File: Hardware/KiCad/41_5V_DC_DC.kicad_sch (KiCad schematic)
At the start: 0 parts

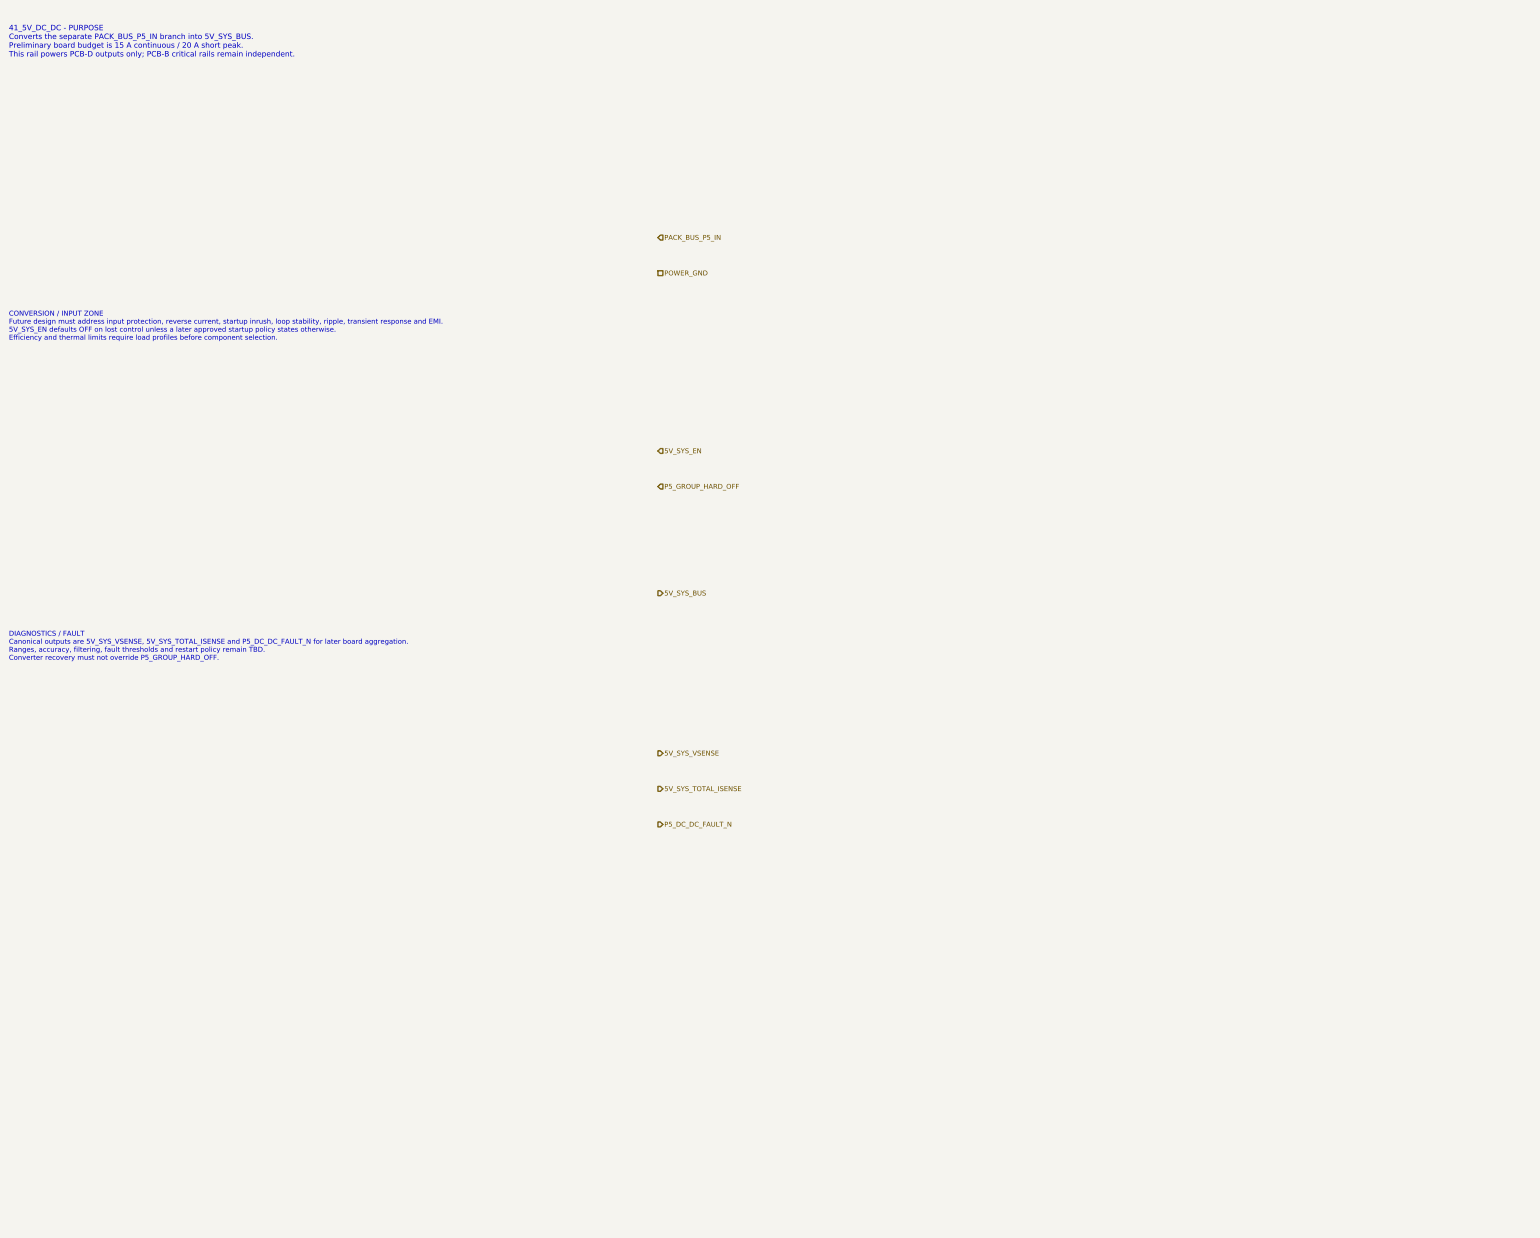
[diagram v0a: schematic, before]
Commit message: hardware: define PCB-D converter core after calculation gate
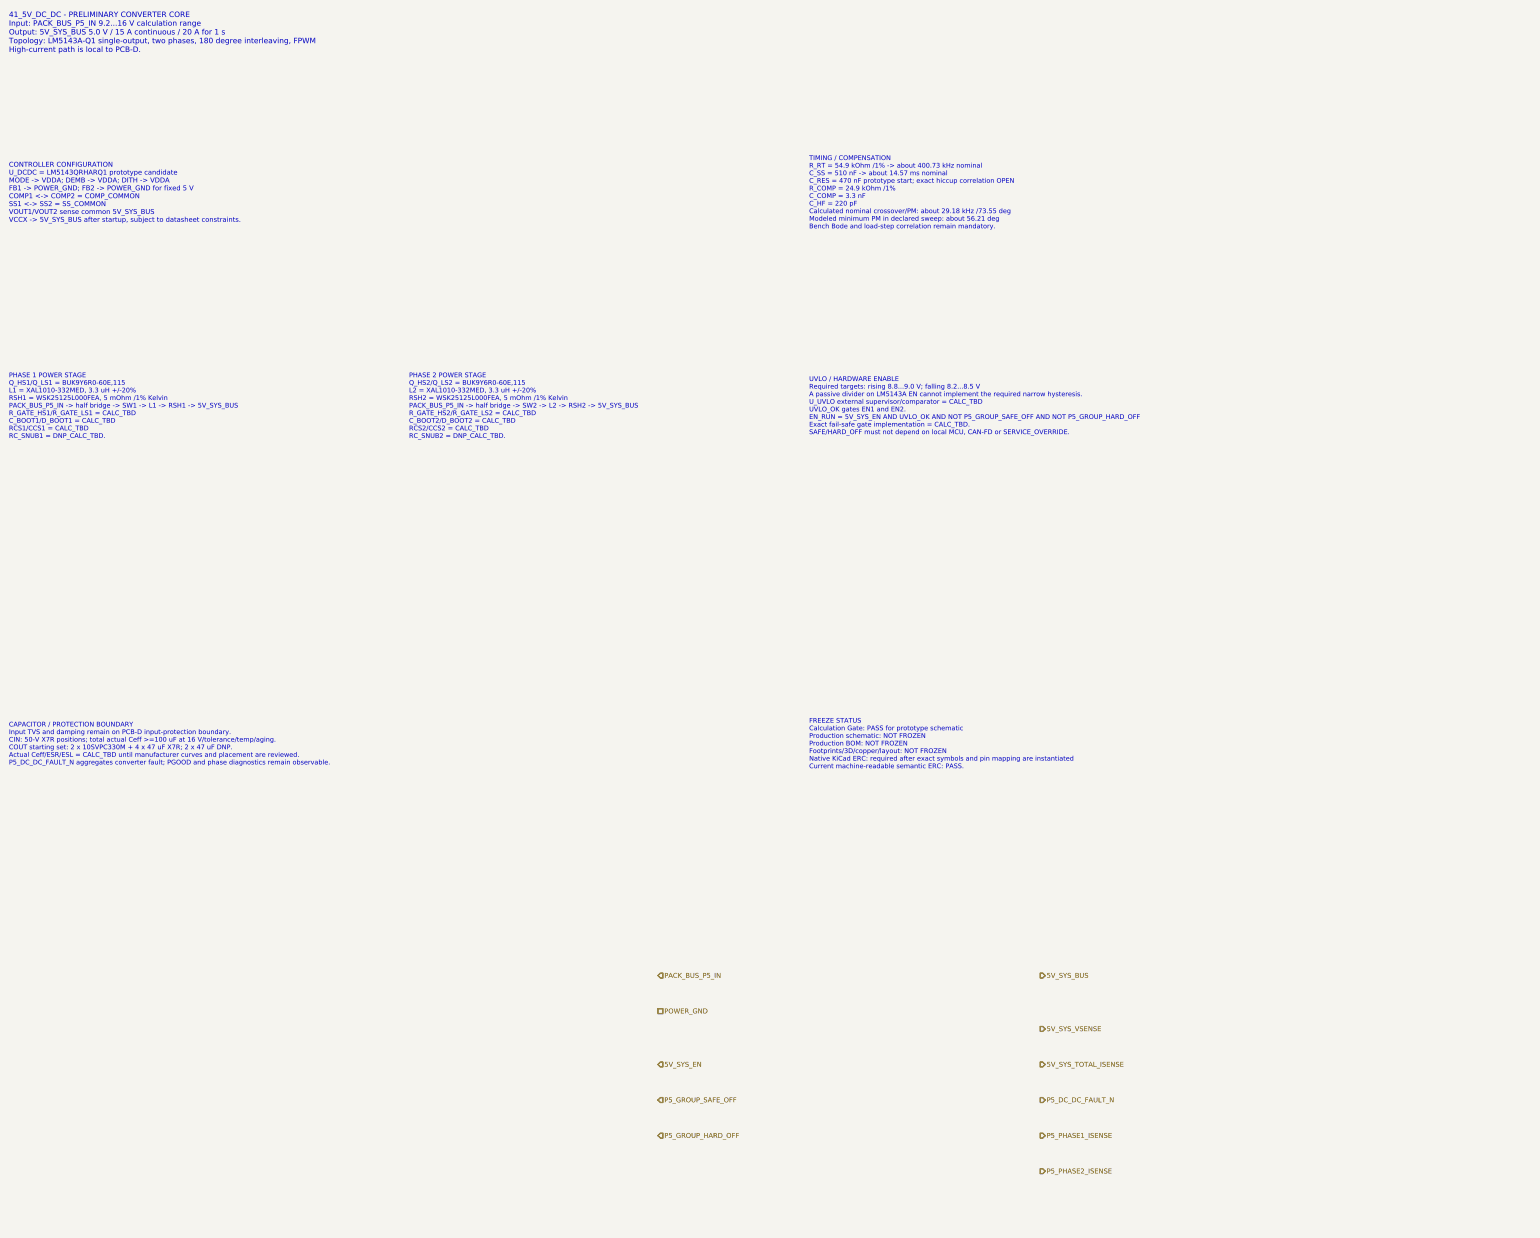
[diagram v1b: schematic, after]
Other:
- note added: "41_5V_DC_DC - PRELIMINARY CONVERTER CORE Input: PACK_BUS_P5_IN 9.2...16 V calculation range Output: 5V_SYS_BUS 5.0 V / 15 A continuous / 20 A for 1 s Topology: LM5143A-Q1 single-output, two phases, 180 degree interleaving, FPWM High-current path is local to PCB-D."
- note added: "CAPACITOR / PROTECTION BOUNDARY Input TVS and damping remain on PCB-D input-protection boundary. CIN: 50-V X7R positions; total actual Ceff >=100 uF at 16 V/tolerance/temp/aging. COUT starting set: 2 x 10SVPC330M + 4 x 47 uF X7R; 2 x 47 uF DNP. Actual Ceff/ESR/ESL = CALC_TBD until manufacturer curves and placement are reviewed. P5_DC_DC_FAULT_N aggregates converter fault; PGOOD and phase diagnost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"
- note added: "CONTROLLER CONFIGURATION U_DCDC = LM5143QRHARQ1 prototype candidate MODE -> VDDA; DEMB -> VDDA; DITH -> VDDA FB1 -> POWER_GND; FB2 -> POWER_GND for fixed 5 V COMP1 <-> COMP2 = COMP_COMMON SS1 <-> SS2 = SS_COMMON VOUT1/VOUT2 sense common 5V_SYS_BUS VCCX -> 5V_SYS_BUS after startup, subject to datasheet constraints."
- note added: "FREEZE STATUS Calculation Gate: PASS for prototype schematic Production schematic: NOT FROZEN Production BOM: NOT FROZEN Footprints/3D/copper/layout: NOT FROZEN Native KiCad ERC: required after exact symbols and pin mapping are instantiated Current machine-readable semantic ERC: PASS."
- note added: "PHASE 1 POWER STAGE Q_HS1/Q_LS1 = BUK9Y6R0-60E,115 L1 = XAL1010-332MED, 3.3 uH +/-20% RSH1 = WSK25125L000FEA, 5 mOhm /1% Kelvin PACK_BUS_P5_IN -> half bridge -> SW1 -> L1 -> RSH1 -> 5V_SYS_BUS R_GATE_HS1/R_GATE_LS1 = CALC_TBD C_BOOT1/D_BOOT1 = CALC_TBD RCS1/CCS1 = CALC_TBD RC_SNUB1 = DNP_CALC_TBD."
- note added: "PHASE 2 POWER STAGE Q_HS2/Q_LS2 = BUK9Y6R0-60E,115 L2 = XAL1010-332MED, 3.3 uH +/-20% RSH2 = WSK25125L000FEA, 5 mOhm /1% Kelvin PACK_BUS_P5_IN -> half bridge -> SW2 -> L2 -> RSH2 -> 5V_SYS_BUS R_GATE_HS2/R_GATE_LS2 = CALC_TBD C_BOOT2/D_BOOT2 = CALC_TBD RCS2/CCS2 = CALC_TBD RC_SNUB2 = DNP_CALC_TBD."
- note added: "TIMING / COMPENSATION R_RT = 54.9 kOhm /1% -> about 400.73 kHz nominal C_SS = 510 nF -> about 14.57 ms nominal C_RES = 470 nF prototype start; exact hiccup correlation OPEN R_COMP = 24.9 kOhm /1% C_COMP = 3.3 nF C_HF = 220 pF Calculated nominal crossover/PM: about 29.18 kHz /73.55 deg Modeled minimum PM in declared sweep: about 56.21 deg Bench Bode and load-step correlation remain mandatory."
- note added: "UVLO / HARDWARE ENABLE Required targets: rising 8.8...9.0 V; falling 8.2...8.5 V A passive divider on LM5143A EN cannot implement the required narrow hysteresis. U_UVLO external supervisor/comparator = CALC_TBD UVLO_OK gates EN1 and EN2. EN_RUN = 5V_SYS_EN AND UVLO_OK AND NOT P5_GROUP_SAFE_OFF AND NOT P5_GROUP_HARD_OFF Exact fail-safe gate implementation = CALC_TBD. SAFE/HARD_OFF must not depend 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"
- note removed: "41_5V_DC_DC - PURPOSE Converts the separate PACK_BUS_P5_IN branch into 5V_SYS_BUS. Preliminary board budget is 15 A continuous / 20 A short peak. This rail powers PCB-D outputs only; PCB-B critical rails remain independent."
- note removed: "CONVERSION / INPUT ZONE Future design must address input protection, reverse current, startup inrush, loop stability, ripple, transient response and EMI. 5V_SYS_EN defaults OFF on lost control unless a later approved startup policy states otherwise. Efficiency and thermal limits require load profiles before component selection."
- note removed: "DIAGNOSTICS / FAULT Canonical outputs are 5V_SYS_VSENSE, 5V_SYS_TOTAL_ISENSE and P5_DC_DC_FAULT_N for later board aggregation. Ranges, accuracy, filtering, fault thresholds and restart policy remain TBD. Converter recovery must not override P5_GROUP_HARD_OFF."
- title: 41_5V_DC_DC - PACK_BUS to 5V_SYS conversion boundary -> 41_5V_DC_DC - PCB-D converter core V1.9
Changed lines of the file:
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@@
 	(paper "A3")
 	(title_block
-		(title "41_5V_DC_DC - PACK_BUS to 5V_SYS conversion boundary")
-		(date "2026-07-15")
-		(rev "B0")
+		(title "41_5V_DC_DC - PCB-D converter core V1.9")
+		(date "2026-07-21")
+		(rev "B1-CALC")
 		(company "Gonoboben/plataVM")
-		(comment 1 "Architecture Level A/B: input protection, DC/DC, enable and primary diagnostics")
-		(comment 2 "No controller, MOSFET, magnetics, capacitor, TVS, sensor or footprint selected")
+		(comment 1 "Prototype converter-core definition after LM5143DESIGN-CALC Gate")
+		(comment 2 "CALC_TBD values explicit; no production BOM, footprints, copper or layout freeze")
 	)
-	(text "41_5V_DC_DC - PURPOSE\nConverts the separate PACK_BUS_P5_IN branch into 5V_SYS_BUS.\nPreliminary board budget is 15 A continuous / 20 A short peak.\nThis rail powers PCB-D outputs only; PCB-B critical rails remain independent."
+	(text "41_5V_DC_DC - PRELIMINARY CONVERTER CORE\nInput: PACK_BUS_P5_IN 9.2...16 V calculation range\nOutput: 5V_SYS_BUS 5.0 V / 15 A continuous / 20 A for 1 s\nTopology: LM5143A-Q1 single-output, two phases, 180 degree interleaving, FPWM\nHigh-current path is local to PCB-D."
 		(exclude_from_sim no)
-		(at 12 14 0)
+		(at 12 12 0)
 		(effects (font (size 1.22 1.22)) (justify left))
 		(uuid "power-5v-00000041-0000-4000-8000-000000000101")
 	)
-	(text "CONVERSION / INPUT ZONE\nFuture design must address input protection, reverse current, startup inrush, loop stability, ripple, transient response and EMI.\n5V_SYS_EN defaults OFF on lost control unless a later approved startup policy states otherwise.\nEfficiency and thermal limits require load profiles before component selection."
+	(text "CONTROLLER CONFIGURATION\nU_DCDC = LM5143QRHARQ1 prototype candidate\nMODE -> VDDA; DEMB -> VDDA; DITH -> VDDA\nFB1 -> POWER_GND; FB2 -> POWER_GND for fixed 5 V\nCOMP1 <-> COMP2 = COMP_COMMON\nSS1 <-> SS2 = SS_COMMON\nVOUT1/VOUT2 sense common 5V_SYS_BUS\nVCCX -> 5V_SYS_BUS after startup, subject to datasheet constraints."
 		(exclude_from_sim no)
-		(at 12 78 0)
-		(effects (font (size 1.12 1.12)) (justify left))
+		(at 12 48 0)
+		(effects (font (size 1.10 1.10)) (justify left))
 		(uuid "power-5v-00000041-0000-4000-8000-000000000102")
 	)
-	(text "DIAGNOSTICS / FAULT\nCanonical outputs are 5V_SYS_VSENSE, 5V_SYS_TOTAL_ISENSE and P5_DC_DC_FAULT_N for later board aggregation.\nRanges, accuracy, filtering, fault thresholds and restart policy remain TBD.\nConverter recovery must not override P5_GROUP_HARD_OFF."
+	(text "PHASE 1 POWER STAGE\nQ_HS1/Q_LS1 = BUK9Y6R0-60E,115\nL1 = XAL1010-332MED, 3.3 uH +/-20%\nRSH1 = WSK25125L000FEA, 5 mOhm /1% Kelvin\nPACK_BUS_P5_IN -> half bridge -> SW1 -> L1 -> RSH1 -> 5V_SYS_BUS\nR_GATE_HS1/R_GATE_LS1 = CALC_TBD\nC_BOOT1/D_BOOT1 = CALC_TBD\nRCS1/CCS1 = CALC_TBD\nRC_SNUB1 = DNP_CALC_TBD."
 		(exclude_from_sim no)
-		(at 12 150 0)
-		(effects (font (size 1.12 1.12)) (justify left))
+		(at 12 96 0)
+		(effects (font (size 1.06 1.06)) (justify left))
 		(uuid "power-5v-00000041-0000-4000-8000-000000000103")
 	)
-	(hierarchical_label "PACK_BUS_P5_IN" (shape input) (exclude_from_sim no) (at 158 58 0) (effects (font (size 1.1 1.1)) (justify left)) (uuid "power-5v-00000041-0000-4000-8000-000000000201"))
-	(hierarchical_label "POWER_GND" (shape passive) (exclude_from_sim no) (at 158 66 0) (effects (font (size 1.1 1.1)) (justify left)) (uuid "power-5v-00000041-0000-4000-8000-000000000202"))
-	(hierarchical_label "5V_SYS_EN" (shape input) (exclude_from_sim no) (at 158 106 0) (effects (font (size 1.1 1.1)) (justify left)) (uuid "power-5v-00000041-0000-4000-8000-000000000203"))
-	(hierarchical_label "P5_GROUP_HARD_OFF" (shape input) (exclude_from_sim no) (at 158 114 0) (effects (font (size 1.1 1.1)) (justify left)) (uuid "power-5v-00000041-0000-4000-8000-000000000204"))
-	(hierarchical_label "5V_SYS_BUS" (shape output) (exclude_from_sim no) (at 158 138 0) (effects (font (size 1.1 1.1)) (justify left)) (uuid "power-5v-00000041-0000-4000-8000-000000000205"))
-	(hierarchical_label "5V_SYS_VSENSE" (shape output) (exclude_from_sim no) (at 158 174 0) (effects (font (size 1.1 1.1)) (justify left)) (uuid "power-5v-00000041-0000-4000-8000-000000000206"))
-	(hierarchical_label "5V_SYS_TOTAL_ISENSE" (shape output) (exclude_from_sim no) (at 158 182 0) (effects (font (size 1.1 1.1)) (justify left)) (uuid "power-5v-00000041-0000-4000-8000-000000000207"))
-	(hierarchical_label "P5_DC_DC_FAULT_N" (shape output) (exclude_from_sim no) (at 158 190 0) (effects (font (size 1.1 1.1)) (justify left)) (uuid "power-5v-00000041-0000-4000-8000-000000000208"))
+	(text "PHASE 2 POWER STAGE\nQ_HS2/Q_LS2 = BUK9Y6R0-60E,115\nL2 = XAL1010-332MED, 3.3 uH +/-20%\nRSH2 = WSK25125L000FEA, 5 mOhm /1% Kelvin\nPACK_BUS_P5_IN -> half bridge -> SW2 -> L2 -> RSH2 -> 5V_SYS_BUS\nR_GATE_HS2/R_GATE_LS2 = CALC_TBD\nC_BOOT2/D_BOOT2 = CALC_TBD\nRCS2/CCS2 = CALC_TBD\nRC_SNUB2 = DNP_CALC_TBD."
+		(exclude_from_sim no)
+		(at 102 96 0)
+		(effects (font (size 1.06 1.06)) (justify left))
+		(uuid "power-5v-00000041-0000-4000-8000-000000000104")
+	)
+	(text "TIMING / COMPENSATION\nR_RT = 54.9 kOhm /1% -> about 400.73 kHz nominal\nC_SS = 510 nF -> about 14.57 ms nominal\nC_RES = 470 nF prototype start; exact hiccup correlation OPEN\nR_COMP = 24.9 kOhm /1%\nC_COMP = 3.3 nF\nC_HF = 220 pF\nCalculated nominal crossover/PM: about 29.18 kHz /73.55 deg\nModeled minimum PM in declared sweep: about 56.21 deg\nBench Bode and load-step correlation remain mandatory."
+		(exclude_from_sim no)
+		(at 192 48 0)
+		(effects (font (size 1.06 1.06)) (justify left))
+		(uuid "power-5v-00000041-0000-4000-8000-000000000105")
+	)
+	(text "UVLO / HARDWARE ENABLE\nRequired targets: rising 8.8...9.0 V; falling 8.2...8.5 V\nA passive divider on LM5143A EN cannot implement the required narrow hysteresis.\nU_UVLO external supervisor/comparator = CALC_TBD\nUVLO_OK gates EN1 and EN2.\nEN_RUN = 5V_SYS_EN AND UVLO_OK AND NOT P5_GROUP_SAFE_OFF AND NOT P5_GROUP_HARD_OFF\nExact fail-safe gate implementation = CALC_TBD.\nSAFE/HARD_OFF must not depend on local MCU, CAN-FD or SERVICE_OVERRIDE."
+		(exclude_from_sim no)
+		(at 192 96 0)
+		(effects (font (size 1.06 1.06)) (justify left))
+		(uuid "power-5v-00000041-0000-4000-8000-000000000106")
+	)
+	(text "CAPACITOR / PROTECTION BOUNDARY\nInput TVS and damping remain on PCB-D input-protection boundary.\nCIN: 50-V X7R positions; total actual Ceff >=100 uF at 16 V/tolerance/temp/aging.\nCOUT starting set: 2 x 10SVPC330M + 4 x 47 uF X7R; 2 x 47 uF DNP.\nActual Ceff/ESR/ESL = CALC_TBD until manufacturer curves and placement are reviewed.\nP5_DC_DC_FAULT_N aggregates converter fault; PGOOD and phase diagnostics remain observable."
+		(exclude_from_sim no)
+		(at 12 172 0)
+		(effects (font (size 1.06 1.06)) (justify left))
+		(uuid "power-5v-00000041-0000-4000-8000-000000000107")
+	)
+	(text "FREEZE STATUS\nCalculation Gate: PASS for prototype schematic\nProduction schematic: NOT FROZEN\nProduction BOM: NOT FROZEN\nFootprints/3D/copper/layout: NOT FROZEN\nNative KiCad ERC: required after exact symbols and pin mapping are instantiated\nCurrent machine-readable semantic ERC: PASS."
+		(exclude_from_sim no)
+		(at 192 172 0)
+		(effects (font (size 1.06 1.06)) (justify left))
+		(uuid "power-5v-00000041-0000-4000-8000-000000000108")
+	)
+	(hierarchical_label "PACK_BUS_P5_IN" (shape input) (exclude_from_sim no) (at 158 224 0) (effects (font (size 1.1 1.1)) (justify left)) (uuid "power-5v-00000041-0000-4000-8000-000000000201"))
+	(hierarchical_label "POWER_GND" (shape passive) (exclude_from_sim no) (at 158 232 0) (effects (font (size 1.1 1.1)) (justify left)) (uuid "power-5v-00000041-0000-4000-8000-000000000202"))
+	(hierarchical_label "5V_SYS_EN" (shape input) (exclude_from_sim no) (at 158 244 0) (effects (font (size 1.1 1.1)) (justify left)) (uuid "power-5v-00000041-0000-4000-8000-000000000203"))
+	(hierarchical_label "P5_GROUP_SAFE_OFF" (shape input) (exclude_from_sim no) (at 158 252 0) (effects (font (size 1.1 1.1)) (justify left)) (uuid "power-5v-00000041-0000-4000-8000-000000000204"))
+	(hierarchical_label "P5_GROUP_HARD_OFF" (shape input) (exclude_from_sim no) (at 158 260 0) (effects (font (size 1.1 1.1)) (justify left)) (uuid "power-5v-00000041-0000-4000-8000-000000000205"))
+	(hierarchical_label "5V_SYS_BUS" (shape output) (exclude_from_sim no) (at 244 224 0) (effects (font (size 1.1 1.1)) (justify left)) (uuid "power-5v-00000041-0000-4000-8000-000000000206"))
+	(hierarchical_label "5V_SYS_VSENSE" (shape output) (exclude_from_sim no) (at 244 236 0) (effects (font (size 1.1 1.1)) (justify left)) (uuid "power-5v-00000041-0000-4000-8000-000000000207"))
+	(hierarchical_label "5V_SYS_TOTAL_ISENSE" (shape output) (exclude_from_sim no) (at 244 244 0) (effects (font (size 1.1 1.1)) (justify left)) (uuid "power-5v-00000041-0000-4000-8000-000000000208"))
+	(hierarchical_label "P5_DC_DC_FAULT_N" (shape output) (exclude_from_sim no) (at 244 252 0) (effects (font (size 1.1 1.1)) (justify left)) (uuid "power-5v-00000041-0000-4000-8000-000000000209"))
+	(hierarchical_label "P5_PHASE1_ISENSE" (shape output) (exclude_from_sim no) (at 244 260 0) (effects (font (size 1.1 1.1)) (justify left)) (uuid "power-5v-00000041-0000-4000-8000-000000000210"))
+	(hierarchical_label "P5_PHASE2_ISENSE" (shape output) (exclude_from_sim no) (at 244 268 0) (effects (font (size 1.1 1.1)) (justify left)) (uuid "power-5v-00000041-0000-4000-8000-000000000211"))
 )
